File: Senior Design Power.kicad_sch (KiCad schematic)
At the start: 21 parts, among them U1 BQ24610

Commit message: 10/23 Commit - Ty
10/23 Commit General schematic completed - Ty
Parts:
- removed R10: R, symbol Device:R
- added C10, C11, C12, C13, C6 (x2), C8, C9: C, symbol Device:C
- added D1: 1N4148WT, Diode_SMD:D_SOD-523, symbol Diode:1N4148WT
- added D3: D_Schottky, symbol Device:D_Schottky
- added L1: L, symbol Device:L
- added Q1, Q2: NMOS, symbol Simulation_SPICE:NMOS
- added R13, R14, R15, RSR: R, symbol Device:R
- added TH1: Thermistor_US, symbol Device:Thermistor_US
- renumbered R8 to R2
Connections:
- net GND: now also C2.2, C3.2, C4.2, U1. (PwrPad), U1.25 (GND), C10.2, C11.2, C13.2, C6.2, C8.1, Q2.3 (S), R15.2, TH1.2
- net at C4.1: now also R2.2, U1.24 (VCC)
- net at R2.1: now also C2.1, C3.1, U1.1 (ACN), U1.2 (ACP), D1.1 (K), Q1.1 (D)
- net at R11.2, R12.1, U1.6 (TS): now also TH1.1
- net at U1.12 (VFB): now also C12.2, R14.2, R15.1
- net Battery Pack +: now reaches U1.13 (SRN)
- net Battery Pack +: now also C10.1, C11.1, C12.1, C9.2, R14.1, RSR.2
- net at U1.14 (SRP): now also C8.2, C9.1, L1.2, RSR.1
- net at U1.17 (GND): now also U1.18 (REGN), C6.1, D3.2 (A)
- net at U1.19 (LODRV): now also Q2.2 (G)
- net at U1.20 (PH): now also C6.1, L1.1, Q1.3 (S), Q2.1 (D)
- net at U1.21 (HIDRV): now also Q1.2 (G)
- net at U1.22 (BTST): now also D3.1 (K), R13.1
- net at U1.7 (TTC): now also C13.1
- net VPULLUP: now reaches R11.1
- new net: C6.2, R13.2
- new net Adapter +: D1.2 (A), R1.1
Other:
- moved on the sheet: C4

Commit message: Nov 4th - All but thermistor R values finished
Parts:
- removed D1: 1N4148WT, Diode_SMD:D_SOD-523, symbol Diode:1N4148WT
- removed R13, R2: R, symbol Device:R
- added C1, C14, C2, C3: 0.1u, symbol Device:C
- added Q1, Q2: PMOS, symbol Simulation_SPICE:PMOS
- added R14, R16: 100k, symbol Device:R
- added R17: 10, symbol Device:R
- added R18: 1k, symbol Device:R
- added RAC: 0.01, symbol Device:R
- C10: renamed from C8; value C -> 0.1u
- C11: renamed from C9; value C -> 0.1u
- C12: renamed from C10; value C -> 20u
- C13: renamed from C11; value C -> 20u
- C16: renamed from C1; value C -> 2.2u
- C4: renamed from C5; value C -> 1u
- C5: renamed from C6; value C -> 1u
- C6: value C -> 0.1u
- C7: renamed from C4; value C -> 1u
- C8: renamed from C2; value C -> 10u
- C9: renamed from C3; value C -> 10u
- CTTC: renamed from C13; value C -> 0.11u
- Cff: renamed from C12; value C -> 22p
- L1: value L -> 3.3u
- R1: renamed from R15; value R -> 10k
- R11: renamed from R7; value R -> 10k
- R12: renamed from R8; value R -> 10k
- R13: renamed from R9; value R -> 10k
- R2: renamed from R14; value R -> 107k
- R20: renamed from R1; value R -> 2
- R5: renamed from R3; value R -> 100k
- R6: value R -> 75k
- R6: renamed from R4; value R -> 25k
- R7: renamed from R5; value R -> 50k
- RSR: value R -> 0.01
- renumbered D3 to D1, D5 to D2, D6 to D3, D7 to D4, Q1 to Q4, Q2 to Q5, R12 to R10, R11 to R9
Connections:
- net Adapter +: now also Q1.1 (D)
- net GND: now also C1.2, C2.2
- net at D1.1 (K), U1.22 (BTST): now also C6.2
- net at R10.1, R9.2, TH1.1: now also R16.2; no longer U1.6 (TS)
- net System: now reaches C7.1, U1.24 (VCC)
- net System: now also C8.1, C9.1, Q4.1 (D), U1.1 (ACN), C3.2, R17.2, RAC.1
- net at U1.3 (~{ACDRV}): now also R18.2
- new net: C2.1, C3.1, Q2.1 (D), RAC.2, U1.2 (ACP)
- new net: C14.2, Q1.2 (G), Q2.2 (G), R14.2, R18.1
- new net: C14.1, Q1.3 (S), Q2.3 (S), R14.1, R17.1
- new net: C1.1, R16.1, U1.6 (TS)
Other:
- moved on the sheet: C11, C16, C9, Cff, R20, RSR

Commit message: 11/5 - PCB created and schematic footprints added
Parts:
- removed D1: D_Schottky, symbol Device:D_Schottky
- removed Q1, Q2: PMOS, symbol Simulation_SPICE:PMOS
- removed Q4, Q5: NMOS, symbol Simulation_SPICE:NMOS
- removed TH1: Thermistor_US, symbol Device:Thermistor_US
- added D1: BAT54J, Diode_SMD:D_SOD-323F, symbol Diode:BAT54J
- added Q1, Q2: Si7617DN, Package_SO:Vishay_PowerPAK_1212-8_Single, symbol Transistor_FET:Si7617DN
- added Q3, Q4: BUK9M85-60EX, Package_TO_SOT_SMD:LFPAK33, symbol Transistor_FET:BUK9M85-60EX
- C1, C11, C12, C13, C14, C2, C3, C4, C5, C6, C7, C8, C9: footprint (none) -> Capacitor_SMD:C_0201_0603Metric
- C10, R1, R10, R11, R12, R13, R14, R16, R17, R18, R2, R20, R5, R6, R7, R9: footprint (none) -> Resistor_SMD:R_0201_0603Metric
- C16, D2, D3, D4: footprint (none) -> LED_SMD:LED_0201_0603Metric
- CTTC1: renamed from CTTC; footprint (none) -> Capacitor_SMD:C_0201_0603Metric
- Cff1: renamed from Cff; footprint (none) -> Capacitor_SMD:C_0201_0603Metric
- L1: footprint (none) -> Inductor_SMD:L_Neosid_SM-PIC0512H
- R4: renamed from R6; footprint (none) -> Resistor_SMD:R_0201_0603Metric
- RAC1: renamed from RAC; footprint (none) -> Resistor_SMD:R_0201_0603Metric
- RSR1: renamed from RSR; footprint (none) -> Resistor_SMD:R_0201_0603Metric
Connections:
- net Adapter +: now also Q1.5 (D)
- net GND: now also Q4.1 (S), Q4.2 (S), Q4.3 (S)
- net System: now also Q3.5 (D)
- net at C6.2, U1.22 (BTST): now also D1.1 (K)
- net at C5.1, U1.17 (GND), U1.18 (REGN): now also D1.2 (A)
- net at C2.1, C3.1, RAC1.2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: now also Q2.5 (D)
- net at C14.2, R14.2, R18.1: now also Q1.4 (G), Q2.4 (G)
- net at C14.1, R14.1, R17.1: now also Q1.1 (S), Q1.2 (S), Q1.3 (S), Q2.1 (S), Q2.2 (S), Q2.3 (S)
- net at C6.1, L1.1, U1.20 (PH): now also Q3.1 (S), Q3.2 (S), Q3.3 (S), Q4.5 (D)
- net Thermistor: now reaches R10.1, R16.2, R9.2
- net at U1.21 (HIDRV): now also Q3.4 (G)
- net at U1.19 (LODRV): now also Q4.4 (G)

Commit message: Nov 7th - changed the footprints & corrected unique parts
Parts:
- D1: footprint Diode_SMD:D_SOD-323F -> DIODE_SOD-523_DIO; symbol Diode:BAT54J -> D1 Senior Design:ZLLS350TA
- L1: footprint Inductor_SMD:L_Neosid_SM-PIC0512H -> L1 Senior Design:IND_IHLP-5050CE_VIS
- Q3: value BUK9M85-60EX -> FDS8447
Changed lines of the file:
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@@
 	)
 	(junction
-		(at 162.56 95.25)
-		(diameter 0)
-		(color 0 0 0 0)
-	)
-	(junction
 		(at 189.23 85.09)
 		(diameter 0)
@@
 	)
 	(junction
-		(at 162.56 87.63)
+		(at 165.1 86.36)
 		(diameter 0)
 		(color 0 0 0 0)
@@
 	)
 	(junction
+		(at 162.56 96.52)
+		(diameter 0)
+		(color 0 0 0 0)
+	)
+	(junction
 		(at 64.77 66.04)
 		(diameter 0)
@@
 	(wire
 		(pts
+			(xy 170.18 87.63) (xy 170.18 86.36)
+		)
+		(stroke
+			(width 0)
+			(type default)
+		)
+	)
+	(wire
+		(pts
+			(xy 170.18 86.36) (xy 165.1 86.36)
+		)
+		(stroke
+			(width 0)
+			(type default)
+		)
+	)
+	(wire
+		(pts
 			(xy 237.49 87.63) (xy 237.49 104.14)
 		)
@@
 	(wire
 		(pts
+			(xy 162.56 96.52) (xy 165.1 96.52)
+		)
+		(stroke
+			(width 0)
+			(type default)
+		)
+	)
+	(wire
+		(pts
 			(xy 101.6 86.36) (xy 129.54 86.36)
 		)
@@
 	(wire
 		(pts
-			(xy 154.94 95.25) (xy 162.56 95.25)
-		)
-		(stroke
-			(width 0)
-			(type default)
-		)
-	)
-	(wire
-		(pts
 			(xy 93.98 101.6) (xy 93.98 104.14)
 		)
@@
 	(wire
 		(pts
+			(xy 158.75 86.36) (xy 165.1 86.36)
+		)
+		(stroke
+			(width 0)
+			(type default)
+		)
+	)
+	(wire
+		(pts
 			(xy 62.23 66.04) (xy 64.77 66.04)
 		)
@@
 	(wire
 		(pts
+			(xy 154.94 95.25) (xy 157.48 95.25)
+		)
+		(stroke
+			(width 0)
+			(type default)
+		)
+	)
+	(wire
+		(pts
 			(xy 120.65 100.33) (xy 129.54 100.33)
 		)
@@
 	(wire
 		(pts
+			(xy 162.56 96.52) (xy 162.56 100.33)
+		)
+		(stroke
+			(width 0)
+			(type default)
+		)
+	)
+	(wire
+		(pts
 			(xy 127 64.77) (xy 127 55.88)
 		)
@@
 	(wire
 		(pts
-			(xy 247.65 106.68) (xy 247.65 104.14)
+			(xy 154.94 87.63) (xy 158.75 87.63)
 		)
 		(stroke
@@
 	(wire
 		(pts
-			(xy 154.94 97.79) (xy 181.61 97.79)
+			(xy 247.65 106.68) (xy 247.65 104.14)
 		)
 		(stroke
@@
 	(wire
 		(pts
-			(xy 162.56 87.63) (xy 177.8 87.63)
+			(xy 154.94 97.79) (xy 181.61 97.79)
 		)
 		(stroke
@@
 	(wire
 		(pts
+			(xy 157.48 96.52) (xy 162.56 96.52)
+		)
+		(stroke
+			(width 0)
+			(type default)
+		)
+	)
+	(wire
+		(pts
 			(xy 64.77 45.72) (xy 128.27 45.72)
 		)
@@
 	(wire
 		(pts
-			(xy 55.88 66.04) (xy 55.88 63.5)
+			(xy 158.75 87.63) (xy 158.75 86.36)
 		)
 		(stroke
@@
 	(wire
 		(pts
-			(xy 129.54 74.93) (xy 127 74.93)
+			(xy 55.88 66.04) (xy 55.88 63.5)
 		)
 		(stroke
@@
 	(wire
 		(pts
-			(xy 107.95 80.01) (xy 107.95 68.58)
+			(xy 129.54 74.93) (xy 127 74.93)
 		)
 		(stroke
@@
 	(wire
 		(pts
-			(xy 154.94 87.63) (xy 162.56 87.63)
+			(xy 107.95 80.01) (xy 107.95 68.58)
 		)
 		(stroke
@@
 	(wire
 		(pts
-			(xy 64.77 55.88) (xy 64.77 45.72)
+			(xy 157.48 95.25) (xy 157.48 96.52)
 		)
 		(stroke
@@
 	(wire
 		(pts
-			(xy 120.65 99.06) (xy 120.65 100.33)
+			(xy 64.77 55.88) (xy 64.77 45.72)
 		)
 		(stroke
@@
 	(wire
 		(pts
-			(xy 189.23 102.87) (xy 189.23 104.14)
+			(xy 120.65 99.06) (xy 120.65 100.33)
 		)
 		(stroke
@@
 	(wire
 		(pts
-			(xy 40.64 55.88) (xy 50.8 55.88)
+			(xy 189.23 102.87) (xy 189.23 104.14)
 		)
 		(stroke
@@
 	(wire
 		(pts
-			(xy 116.84 55.88) (xy 118.11 55.88)
+			(xy 40.64 55.88) (xy 50.8 55.88)
 		)
 		(stroke
@@
 	(wire
 		(pts
-			(xy 162.56 95.25) (xy 162.56 100.33)
+			(xy 116.84 55.88) (xy 118.11 55.88)
 		)
 		(stroke
@@
 	(wire
 		(pts
+			(xy 177.8 87.63) (xy 170.18 87.63)
+		)
+		(stroke
+			(width 0)
+			(type default)
+		)
+	)
+	(wire
+		(pts
 			(xy 66.04 123.19) (xy 66.04 130.81)
 		)
@@
 			)
 		)
-		(property "Footprint" "Inductor_SMD:L_Neosid_SM-PIC0512H"
+		(property "Footprint" "L1 Senior Design:IND_IHLP-5050CE_VIS"
 			(at 204.47 87.63 0)
 			(effects
@@
 			)
 		)
-		(property "Value" "BUK9M85-60EX"
+		(property "Value" "FDS8447"
 			(at 193.04 80.0099 0)
 			(effects
@@
 			)
 		)
-		(property "Datasheet" "https://assets.nexperia.com/documents/data-sheet/BUK9M85-60E.pdf"
+		(property "Datasheet" "https://www.onsemi.com/pdf/datasheet/fds8447-d.pdf"
 			(at 191.77 82.55 0)
 			(effects
@@
 			)
 		)
-		(property "Description" "12.8A Id, 60V Vds, N-Channel TrenchMOS MOSFET, 73mOhm Ron, 4.4nC Qqd, -55 to 175 °C, LFPAK33"
+		(property "Description" "12.8A Id, 40V Vds, N-Channel TrenchMOS MOSFET, 10.5mOhm Ron, 7nC Qqd, -55 to 150 °C, LFPAK33"
 			(at 186.69 78.74 0)
 			(effects
@@
 	)
 	(symbol
-		(lib_id "Diode:BAT54J")
-		(at 162.56 91.44 270)
+		(lib_id "D1 Senior Design:ZLLS350TA")
+		(at 165.1 96.52 90)
 		(unit 1)
 		(exclude_from_sim no)
@@
 		(fields_autoplaced yes)
 		(property "Reference" "D1"
-			(at 165.1 89.8524 90)
+			(at 168.91 90.1699 90)
 			(effects
 				(font
 					(size 1.27 1.27)
 				)
-				(justify left)
+				(justify right)
 			)
 		)
 		(property "Value" "BAT54J"
-			(at 165.1 92.3924 90)
+			(at 168.91 92.7099 90)
 			(effects
 				(font
 					(size 1.27 1.27)
 				)
-				(justify left)
+				(justify right)
 			)
 		)
-		(property "Footprint" "Diode_SMD:D_SOD-323F"
-			(at 158.115 91.44 0)
+		(property "Footprint" "DIODE_SOD-523_DIO"
+			(at 165.1 96.52 0)
 			(effects
 				(font
 					(size 1.27 1.27)
+					(italic yes)
 				)
 				(hide yes)
 			)
 		)
-		(property "Datasheet" "https://assets.nexperia.com/documents/data-sheet/BAT54J.pdf"
-			(at 162.56 91.44 0)
+		(property "Datasheet" "ZLLS350TA"
+			(at 165.1 96.52 0)
 			(effects
 				(font
 					(size 1.27 1.27)
+					(italic yes)
 				)
 				(hide yes)
@@
 		)
 		(property "Description" "30V 200mA Schottky diode, SOD-323F"
-			(at 162.56 91.44 0)
+			(at 165.1 96.52 0)
 			(effects
 				(font

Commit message: Nov 13th - Ty
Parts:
- removed Q3: FDS8447, Package_TO_SOT_SMD:LFPAK33, symbol Transistor_FET:BUK9M85-60EX
- removed Q4: BUK9M85-60EX, Package_TO_SOT_SMD:LFPAK33, symbol Transistor_FET:BUK9M85-60EX
- added C15, C17: C, symbol Device:C
- added Q3, Q4: SIS412DN, Q3/4 Senior Design:POWERPAK_1212-8, symbol Simulation_SPICE:NMOS
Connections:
- net GND: now also Q4.3 (S)
- net System: now also Q3.1 (D)
- net at C6.1, L1.1, U1.20 (PH): now also Q3.3 (S), Q4.1 (D)
- net at U1.19 (LODRV): now also Q4.2 (G)
- net at U1.21 (HIDRV): now also Q3.2 (G)

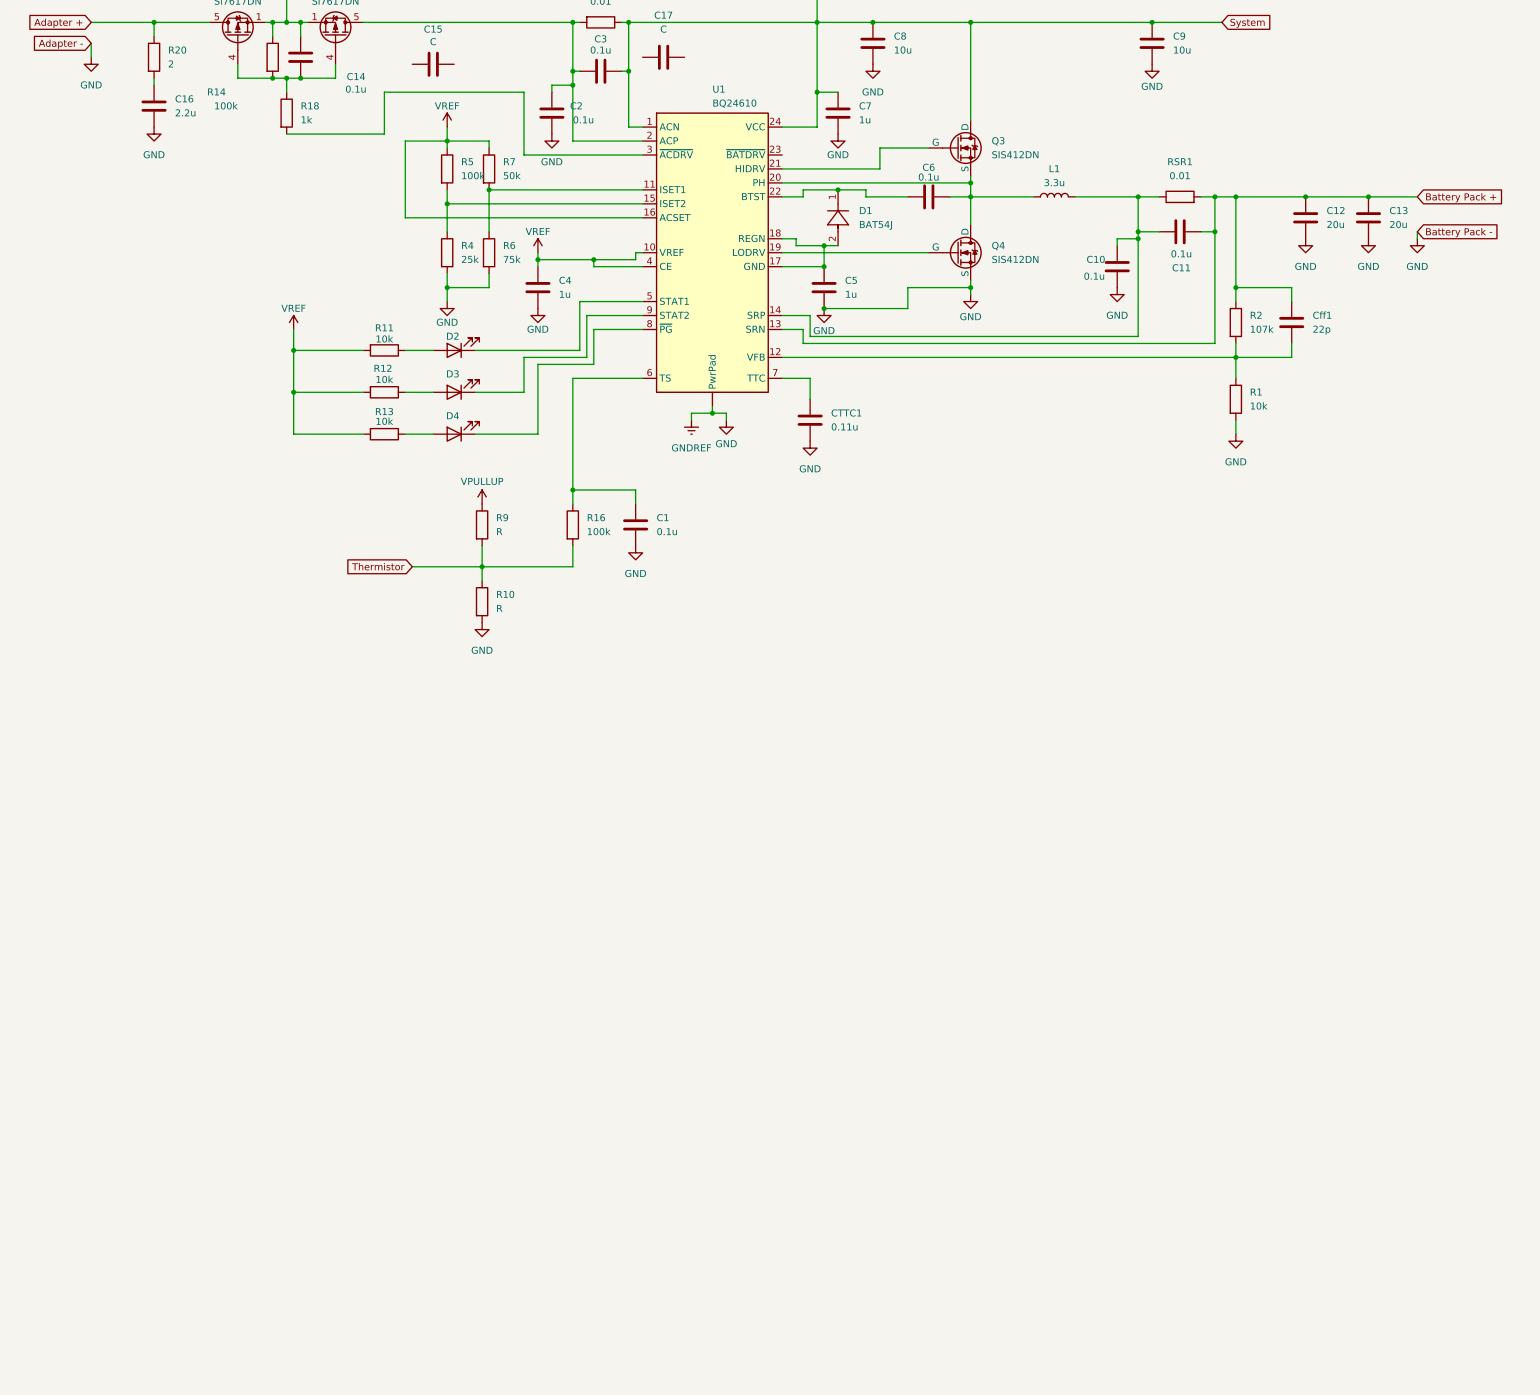
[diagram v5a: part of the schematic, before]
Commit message: adding evm board parts to schematic
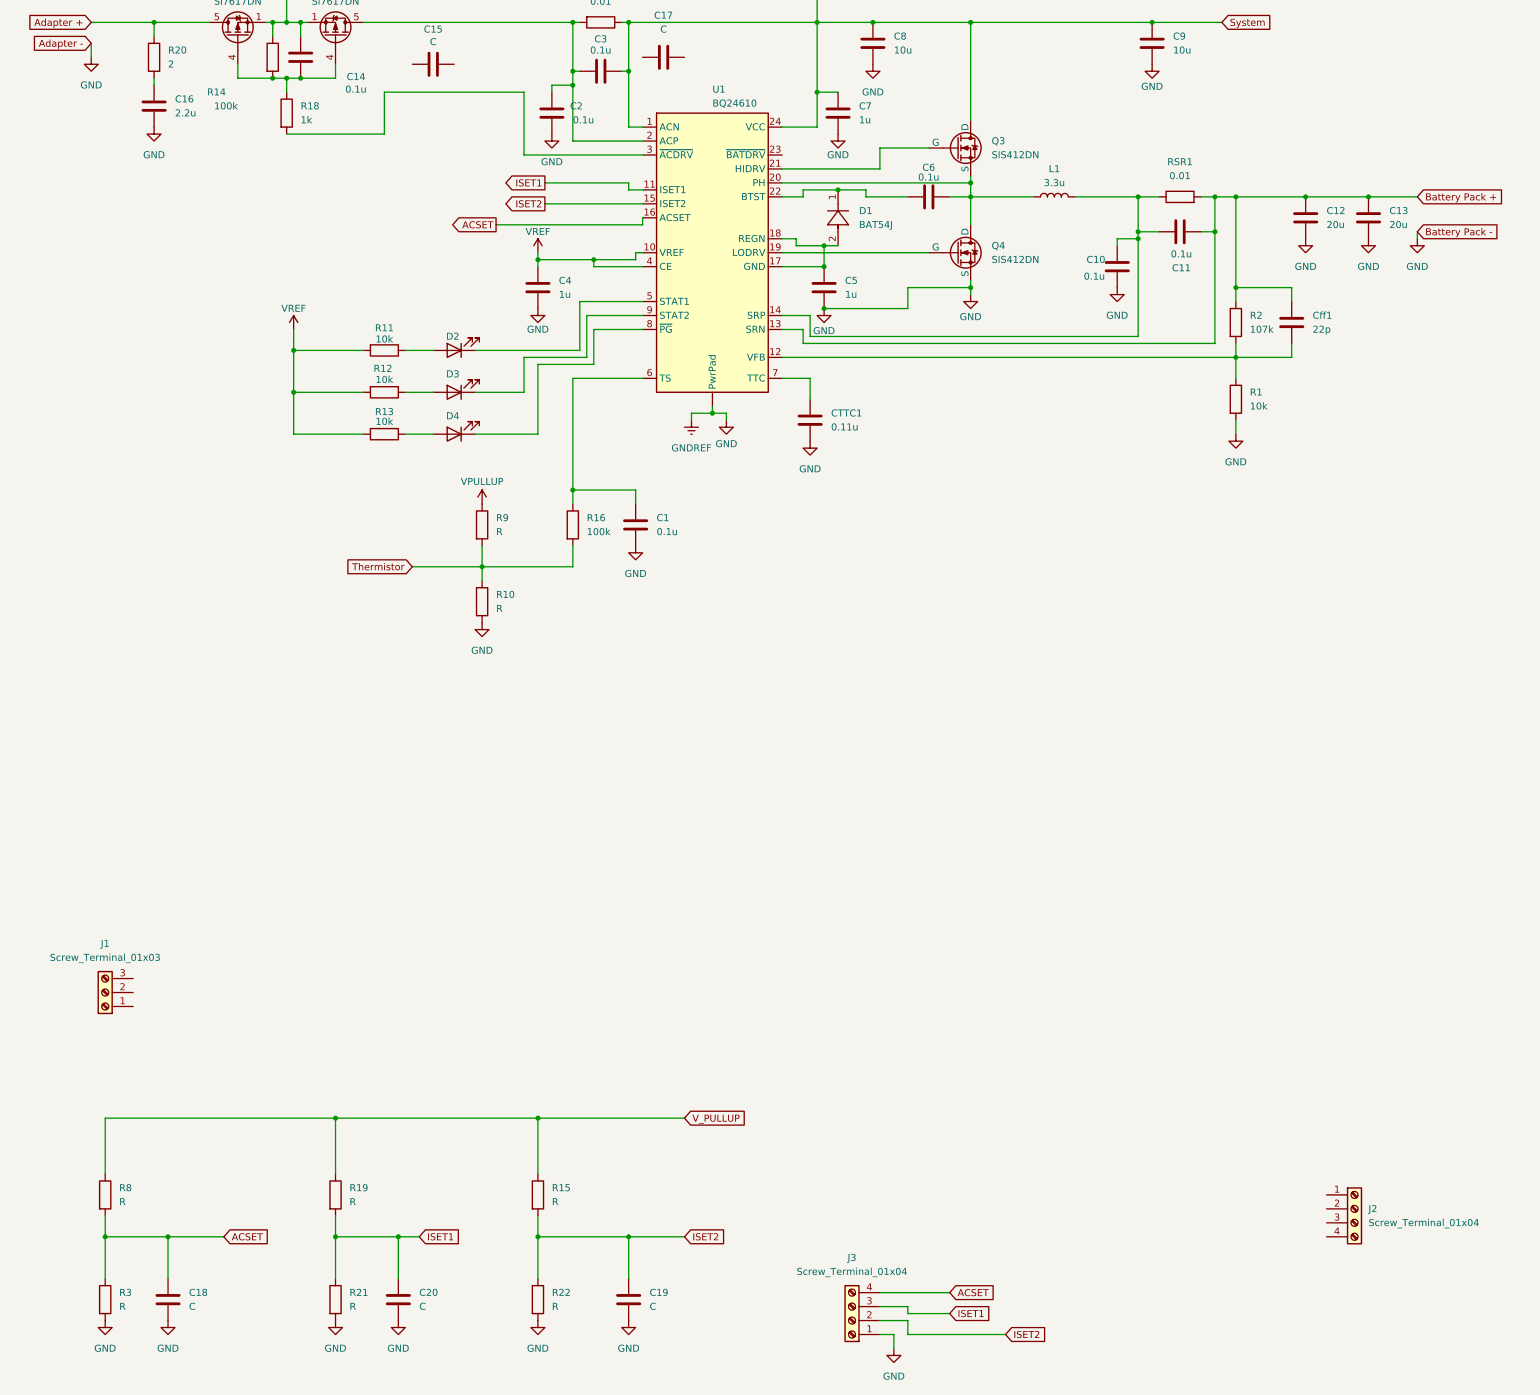
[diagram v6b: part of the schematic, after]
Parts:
- removed R4: 25k, Resistor_SMD:R_0201_0603Metric, symbol Device:R
- removed R5: 100k, Resistor_SMD:R_0201_0603Metric, symbol Device:R
- removed R6: 75k, Resistor_SMD:R_0201_0603Metric, symbol Device:R
- removed R7: 50k, Resistor_SMD:R_0201_0603Metric, symbol Device:R
- added C18, C19, C20: C, symbol Device:C
- added J1: Screw_Terminal_01x03, symbol Connector:Screw_Terminal_01x03
- added J2, J3: Screw_Terminal_01x04, symbol Connector:Screw_Terminal_01x04
- added R15, R19, R21, R22, R3, R8: R, symbol Device:R
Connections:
- net GND: now also C18.2, C19.2, C20.2, J3.1 (Pin_1), R21.2, R22.2, R3.2
- net VREF: no longer U1.16 (ACSET)
- net ISET1: now reaches U1.11 (ISET1)
- net ISET1: now also C20.1, J3.3 (Pin_3), R19.2, R21.1
- net ISET2: now reaches U1.15 (ISET2)
- net ISET2: now also C19.1, J3.2 (Pin_2), R15.2, R22.1
- new net ACSET: C18.1, J3.4 (Pin_4), R3.1, R8.2, U1.16 (ACSET)
- new net V_PULLUP: R15.1, R19.1, R8.1
